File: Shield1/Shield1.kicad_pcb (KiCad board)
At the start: 4 copper layers, 12 x 19 mm, 26 parts, among them J1 Conn_01x01_Male, J10 Conn_01x01_Male, J11 Conn_01x01_Male, J12 Conn_01x01_Male, J13 Conn_01x01_Male, J14 Conn_01x01_Male, J15 Conn_01x01_Male, J17 Conn_01x01_Male, J2 Conn_01x01_Male, J25 Conn_01x01_Male, J26 Conn_01x01_Male, J27 Conn_01x01_Male, J28 Conn_01x01_Male, J29 Conn_01x01_Male, J3 Conn_01x01_Male, J5 Conn_01x01_Male, J6 Conn_01x01_Male, J7 Conn_01x01_Male, J8 Conn_01x01_Male, J9 Conn_01x01_Male, X1 USB_C_24pins

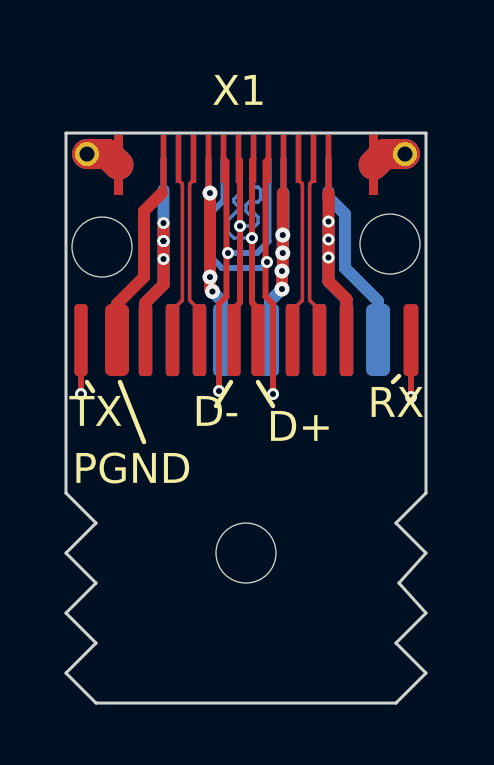
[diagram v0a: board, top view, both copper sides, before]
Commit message: v0.99 GND has been corrected
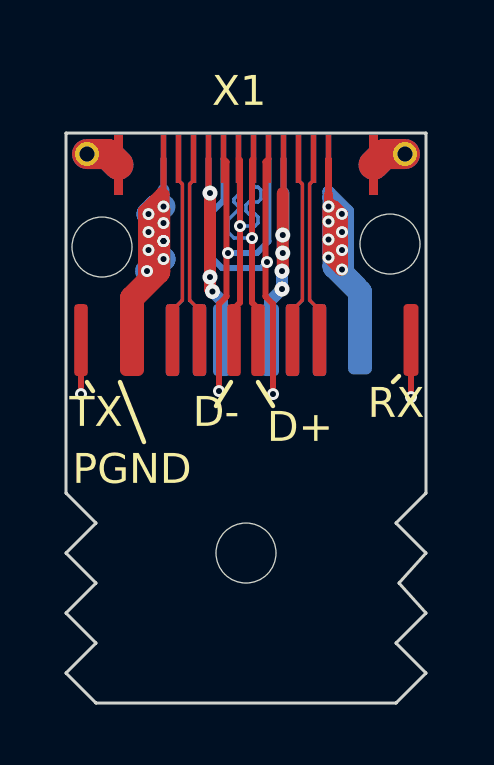
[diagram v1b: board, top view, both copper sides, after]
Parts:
- removed J26, J27, J28, J29: Conn_01x01_Male, Shield1:smdPin
- moved ? 0.60 mm to (103.8, 26.9)
- moved ? 0.50 mm to (96.2, 26.9)
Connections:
- X1 pad 0: Earth -> (no net)
- X1 pad A1: GND1 -> GND3
- X1 pad B1: GND2 -> GND
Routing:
- net GND: track 6.72 -> 28.1 mm, vias 0 -> 8
- net GND3: track 6.68 -> 20.6 mm, vias 0 -> 9
- net GND2: track 10.6 -> 0.00 mm, vias 3 -> 0
- net GND1: track 10.4 -> 0.00 mm, vias 4 -> 0
- added copper zone on In1.Cu, net GND
- added copper zone on In2.Cu, net GND
- added copper zone on In1.Cu, net GND3
- added copper zone on In2.Cu, net GND3
- removed copper zone on In1.Cu, net GND1
- removed copper zone on In2.Cu, net GND1
- removed copper zone on In1.Cu, net GND2
- removed copper zone on In2.Cu, net GND2

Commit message: v1.0 Penny 3 to Rezonit!
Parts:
- moved J2 0.25 mm to (101.5, 26.9)
- moved J1 0.23 mm to (98.5, 26.8)
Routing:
- net VBUS1: track 7.40 -> 9.24 mm, vias 3 -> 2
- net VBUS2: track 9.48 -> 10.7 mm
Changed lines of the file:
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@@
       (effects (font (size 1.27 1.27) (thickness 0.15)))
     )
-    (pad "1" smd roundrect (at 0 0 180) (size 0.8 2.4) (layers "F.Cu" "F.Paste" "F.Mask") (roundrect_rratio 0.25)
+    (pad "1" smd roundrect (at 0 0 180) (size 1.2 2.4) (layers "F.Cu" "F.Paste" "F.Mask") (roundrect_rratio 0.25)
       (net 17 "GND3") (pinfunction "Pin_1") (pintype "passive"))
   )
@@
   )
   (footprint "Shield1:smdPin" (layer "B.Cu")
-    (at 101.725 26.87 180)
+    (at 101.475 26.87 180)
     (property "Sheetfile" "Shield1.kicad_sch")
     (property "Sheetname" "")
@@
       (effects (font (size 1 1) (thickness 0.15)) (justify mirror))
     )
-    (pad "1" smd roundrect (at 0.925 -0.03) (size 0.6 2.4) (layers "B.Cu" "B.Paste" "B.Mask") (roundrect_rratio 0.25)
+    (pad "1" smd roundrect (at 0.925 -0.03) (size 0.8 2.4) (layers "B.Cu" "B.Paste" "B.Mask") (roundrect_rratio 0.25)
       (net 3 "VBUS2") (pinfunction "Pin_1") (pintype "passive"))
   )
@@
   )
   (footprint "Shield1:smdPin" (layer "B.Cu")
-    (at 98.28 26.83 180)
+    (at 98.515 26.83 180)
     (property "Sheetfile" "Shield1.kicad_sch")
     (property "Sheetname" "")
@@
       (effects (font (size 1 1) (thickness 0.15)) (justify mirror))
     )
-    (pad "1" smd roundrect (at -0.92 -0.07) (size 0.6 2.4) (layers "B.Cu" "B.Paste" "B.Mask") (roundrect_rratio 0.25)
+    (pad "1" smd roundrect (at -0.92 -0.07) (size 0.8 2.4) (layers "B.Cu" "B.Paste" "B.Mask") (roundrect_rratio 0.25)
       (net 2 "VBUS1") (pinfunction "Pin_1") (pintype "passive"))
   )
@@
       (effects (font (size 1.27 1.27) (thickness 0.15)) (justify mirror))
     )
-    (pad "1" smd roundrect (at 0 0) (size 0.8 2.4) (layers "B.Cu" "B.Paste" "B.Mask") (roundrect_rratio 0.25)
+    (pad "1" smd roundrect (at 0 0) (size 1.2 2.4) (layers "B.Cu" "B.Paste" "B.Mask") (roundrect_rratio 0.25)
       (net 16 "GND") (pinfunction "Pin_1") (pintype "passive"))
   )
@@
   )
   (dimension (type aligned) (layer "Dwgs.User")
+    (pts (xy 106 20) (xy 106 39.1))
+    (height -3.73)
+    (gr_text "19.1000 мм" (at 108.58 29.55 90) (layer "Dwgs.User")
+      (effects (font (size 1 1) (thickness 0.15)))
+    )
+    (format (units 3) (units_format 1) (precision 4))
+    (style (thickness 0.1) (arrow_length 1.27) (text_position_mode 0) (extension_height 0.58642) (extension_offset 0.5) keep_text_aligned)
+  )
+  (dimension (type aligned) (layer "Dwgs.User")
     (pts (xy 100 31.3) (xy 100 39))
     (height 10.4)
@@
     (style (thickness 0.15) (arrow_length 1.27) (text_position_mode 0) (extension_height 0.58642) (extension_offset 0.5) keep_text_aligned)
   )
-  (dimension (type aligned) (layer "Edge.Cuts")
-    (pts (xy 106 20) (xy 106 39.1))
-    (height -3.73)
-    (gr_text "19.1000 мм" (at 108.58 29.55 90) (layer "Edge.Cuts")
-      (effects (font (size 1 1) (thickness 0.15)))
-    )
-    (format (units 3) (units_format 1) (precision 4))
-    (style (thickness 0.1) (arrow_length 1.27) (text_position_mode 0) (extension_height 0.58642) (extension_offset 0.5) keep_text_aligned)
-  )
-  (dimension (type aligned) (layer "Edge.Cuts")
+  (dimension (type aligned) (layer "Dwgs.User")
     (pts (xy 94 38.85) (xy 106 38.85))
     (height 5.95)
-    (gr_text "12.0000 мм" (at 99.9 46.3) (layer "Edge.Cuts")
+    (gr_text "12.0000 мм" (at 99.9 46.3) (layer "Dwgs.User")
       (effects (font (size 1 1) (thickness 0.15)))
     )
@@
   (segment (start 105.3 20.7) (end 104.61 20.7) (width 1) (layer "B.Cu") (net 1))
   (segment (start 95.39 20.7) (end 95.75 21.06) (width 1) (layer "B.Cu") (net 1))
-  (segment (start 98.8 24.8) (end 98.8 25.2) (width 0.4) (layer "F.Cu") (net 2))
+  (segment (start 98.8 25.2) (end 98.8 22) (width 0.4) (layer "F.Cu") (net 2))
   (segment (start 98.75 20.86) (end 98.75 22) (width 0.2) (layer "F.Cu") (net 2))
-  (segment (start 98.8 25.2) (end 98.882155 25.282155) (width 0.4) (layer "F.Cu") (net 2))
-  (segment (start 98.8 24.8) (end 98.8 22) (width 0.4) (layer "F.Cu") (net 2))
+  (segment (start 98.882155 25.282155) (end 98.8 25.2) (width 0.4) (layer "F.Cu") (net 2))
   (via (at 98.8 22) (size 0.5) (drill 0.2) (layers "F.Cu" "B.Cu") (net 2))
-  (via (at 98.8 24.8) (size 0.5) (drill 0.2) (layers "F.Cu" "B.Cu") (net 2))
   (via (at 98.882155 25.282155) (size 0.5) (drill 0.2) (layers "F.Cu" "B.Cu") (net 2))
   (segment (start 98.8 22) (end 98.75 22) (width 0.4) (layer "B.Cu") (net 2))
   (segment (start 98.75 20.86) (end 98.75 22) (width 0.2) (layer "B.Cu") (net 2))
-  (segment (start 99.2 25.7) (end 99.2 26.9) (width 0.2) (layer "B.Cu") (net 2))
+  (segment (start 99.2 25.7) (end 99.2 26.9) (width 0.4) (layer "B.Cu") (net 2))
   (segment (start 98.882155 25.282155) (end 99.2 25.6) (width 0.4) (layer "B.Cu") (net 2))
+  (segment (start 99.435 25.835) (end 98.882155 25.282155) (width 0.3) (layer "B.Cu") (net 2))
   (segment (start 99.2 25.6) (end 99.2 25.7) (width 0.4) (layer "B.Cu") (net 2))
-  (segment (start 101.225499 24.574501) (end 101.2 24.6) (width 0.4) (layer "F.Cu") (net 3))
+  (segment (start 99.435 26.9) (end 99.435 25.835) (width 0.3) (layer "B.Cu") (net 2))
+  (segment (start 101.2 24.025499) (end 101.225499 24) (width 0.3) (layer "F.Cu") (net 3))
   (segment (start 101.25 21.975499) (end 101.225499 22) (width 0.2) (layer "F.Cu") (net 3))
-  (segment (start 101.225499 24) (end 101.225499 24.574501) (width 0.4) (layer "F.Cu") (net 3))
   (segment (start 101.225499 23.4) (end 101.225499 22) (width 0.4) (layer "F.Cu") (net 3))
   (segment (start 101.25 20.86) (end 101.25 21.975499) (width 0.2) (layer "F.Cu") (net 3))
   (segment (start 101.225499 24) (end 101.225499 23.4) (width 0.4) (layer "F.Cu") (net 3))
+  (segment (start 101.2 25.2) (end 101.2 24.025499) (width 0.4) (layer "F.Cu") (net 3))
   (via (at 101.2 25.2) (size 0.5) (drill 0.2) (layers "F.Cu" "B.Cu") (net 3))
   (via (at 101.2 24.6) (size 0.5) (drill 0.2) (layers "F.Cu" "B.Cu") (net 3))
   (via (at 101.225499 24) (size 0.5) (drill 0.2) (layers "F.Cu" "B.Cu") (net 3))
   (via (at 101.225499 23.4) (size 0.5) (drill 0.2) (layers "F.Cu" "B.Cu") (net 3))
+  (segment (start 101.2 24.025499) (end 101.225499 24) (width 0.3) (layer "B.Cu") (net 3))
   (segment (start 101.2 25.2) (end 100.8 25.6) (width 0.4) (layer "B.Cu") (net 3))
   (segment (start 101.225499 23.425499) (end 101.25 23.45) (width 0.2) (layer "B.Cu") (net 3))
@@
   (segment (start 100.8 25.6) (end 100.8 25.7) (width 0.4) (layer "B.Cu") (net 3))
   (segment (start 101.2 25.2) (end 101.2 24.6) (width 0.4) (layer "B.Cu") (net 3))
-  (segment (start 100.8 25.7) (end 100.8 26.9) (width 0.2) (layer "B.Cu") (net 3))
+  (segment (start 100.8 25.7) (end 100.8 26.9) (width 0.4) (layer "B.Cu") (net 3))
   (segment (start 101.25 20.86) (end 101.25 22) (width 0.2) (layer "B.Cu") (net 3))
   (segment (start 101.225499 23.4) (end 101.225499 23.425499) (width 0.2) (layer "B.Cu") (net 3))
+  (segment (start 101.2 24.6) (end 101.2 24.025499) (width 0.4) (layer "B.Cu") (net 3))
   (segment (start 99.8 25.5) (end 99.8 25.65) (width 0.2) (layer "F.Cu") (net 4))
   (segment (start 99.8 25.65) (end 99.6 25.85) (width 0.2) (layer "F.Cu") (net 4))
@@
   (via (at 96.75 22.7) (size 0.4) (drill 0.2) (layers "F.Cu" "B.Cu") (net 17))
   (via (at 96.75 23.3) (size 0.4) (drill 0.2) (layers "F.Cu" "B.Cu") (net 17))
-  (via (at 97.25 23.6) (size 0.4) (drill 0.2) (layers "F.Cu" "B.Cu") (net 17))
-  (via (at 97.25 23.6) (size 0.4) (drill 0.2) (layers "F.Cu" "B.Cu") (net 17))
+  (via (at 97.25 23.55) (size 0.4) (drill 0.2) (layers "F.Cu" "B.Cu") (net 17))
+  (via (at 97.25 23.55) (size 0.4) (drill 0.2) (layers "F.Cu" "B.Cu") (net 17))
   (via (at 97.25 23) (size 0.4) (drill 0.2) (layers "F.Cu" "B.Cu") (net 17))
   (via (at 97.25 22.45) (size 0.4) (drill 0.2) (layers "F.Cu" "B.Cu") (net 17))
+  (segment (start 97.25 24.2) (end 97.25 23.55) (width 0.4) (layer "B.Cu") (net 17))
   (segment (start 96.75 22.7) (end 96.799521 22.749521) (width 0.8) (layer "B.Cu") (net 17))
   (segment (start 96.75 24.55) (end 96.7 24.6) (width 0.4) (layer "B.Cu") (net 17))
-  (segment (start 97.25 24.2) (end 97.25 23.6) (width 0.4) (layer "B.Cu") (net 17))
   (segment (start 97.099521 24.2) (end 96.799521 23.9) (width 0.8) (layer "B.Cu") (net 17))
   (segment (start 96.75 23.9) (end 96.75 24.55) (width 0.4) (layer "B.Cu") (net 17))
+  (segment (start 97.25 23.55) (end 97.25 23) (width 0.4) (layer "B.Cu") (net 17))
   (segment (start 97.25 24.2) (end 97.099521 24.2) (width 0.8) (layer "B.Cu") (net 17))
   (segment (start 97.1 24.2) (end 96.7 24.6) (width 0.8) (layer "B.Cu") (net 17))
-  (segment (start 97.25 23.6) (end 97.25 23) (width 0.4) (layer "B.Cu") (net 17))
   (segment (start 97.25 20.86) (end 97.25 21.9) (width 0.2) (layer "B.Cu") (net 17))
   (segment (start 96.799521 22.749521) (end 96.799521 23.9) (width 0.8) (layer "B.Cu") (net 17))
